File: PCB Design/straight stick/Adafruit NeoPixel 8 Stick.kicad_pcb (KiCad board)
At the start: 2 copper layers, 52.3 x 15.7 mm, 22 parts, among them CN1 1X4SMT, CN2 1X4SMT, J1 2058703-2, J2 2058703-2

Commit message: cleaner routing
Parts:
- removed J1, J2: 2058703-2, 2058703-2:TE_2058703-2
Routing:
- net GND: track 50.3 -> 18.4 mm, vias 10 -> 7
- net +5V: track 113.2 -> 110.4 mm, vias 7 -> 3

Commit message: 4 pin fix
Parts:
- removed C1, C2, C3, C4, C5, C6, C7, C8: C-USC0805K, Adafruit NeoPixel 8 Stick:C0805K
- removed LED1, LED2, LED3, LED4, LED5, LED6, LED7, LED8: >VALUE, Adafruit NeoPixel 8 Stick:WS28115050
- added D1: WS2812B, LED_SMD:LED_WS2812B_PLCC4_5.0x5.0mm_P3.2mm, F.Cu at (126.5, 105.2)
- added D2: WS2812B, LED_SMD:LED_WS2812B_PLCC4_5.0x5.0mm_P3.2mm, F.Cu at (133.6, 105.2)
- added D3: WS2812B, LED_SMD:LED_WS2812B_PLCC4_5.0x5.0mm_P3.2mm, F.Cu at (140.7, 105.2)
- added D4: WS2812B, LED_SMD:LED_WS2812B_PLCC4_5.0x5.0mm_P3.2mm, F.Cu at (147.8, 105.2)
- added D5: WS2812B, LED_SMD:LED_WS2812B_PLCC4_5.0x5.0mm_P3.2mm, F.Cu at (154.9, 105.2)
- added D6: WS2812B, LED_SMD:LED_WS2812B_PLCC4_5.0x5.0mm_P3.2mm, F.Cu at (162.1, 105.2)
- added D7: WS2812B, LED_SMD:LED_WS2812B_PLCC4_5.0x5.0mm_P3.2mm, F.Cu at (169.2, 105.2)
- added D8: WS2812B, LED_SMD:LED_WS2812B_PLCC4_5.0x5.0mm_P3.2mm, F.Cu at (176.3, 105.2)
- moved CN1 5.59 mm to (176.3, 104.4)
- moved FID1 4.70 mm to (133.1, 101.1)
- moved FID3 1.61 mm to (169.7, 101.1)
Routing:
- net +5V: track 110.4 -> 71.8 mm, vias 3 -> 2
- net GND: track 18.4 -> 0.00 mm, vias 7 -> 1
- net Net-(CN1-Pad2): track 18.1 -> 2.63 mm
- net Net-(LED4-PadDO): track 9.64 -> 0.00 mm
- net Net-(LED3-PadDO): track 9.64 -> 0.00 mm
- net Net-(LED2-PadDO): track 9.64 -> 0.00 mm
- net Net-(LED1-PadDO): track 9.64 -> 0.00 mm
- net Net-(LED5-PadDO): track 9.57 -> 0.00 mm
- net Net-(LED7-PadDO): track 9.02 -> 0.00 mm
- net Net-(LED6-PadDO): track 8.87 -> 0.00 mm
- net Net-(D5-Pad2): track 0.00 -> 4.12 mm
- net Net-(D4-Pad2): track 0.00 -> 4.12 mm
- net Net-(D7-Pad2): track 0.00 -> 4.12 mm
- net Net-(D6-Pad2): track 0.00 -> 4.12 mm
- net Net-(D3-Pad2): track 0.00 -> 4.12 mm
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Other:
- board size 52.3 x 15.7 mm -> 57.9 x 15.7 mm

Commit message: 6 pin
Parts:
- removed FID1, FID3: FIDUCIAL"", Adafruit NeoPixel 8 Stick:FIDUCIAL_1MM
- moved CN1 4.06 mm to (176.1, 108.5)
- moved D1 2.79 mm to (126.5, 108.0)
- moved D2 2.79 mm to (133.6, 108.0)
- moved D3 2.79 mm to (140.7, 108.0)
- moved D4 2.79 mm to (147.8, 108.0)
- moved D5 2.79 mm to (154.9, 108.0)
- moved D6 2.79 mm to (162.1, 108.0)
- moved D7 2.79 mm to (169.2, 108.0)
- moved D8 2.79 mm to (176.3, 108.0)
- moved CN2 1.53 mm to (126.9, 107.4)
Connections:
- CN1 pad 1: GND -> Net-(CN1-Pad1)
- CN1 pad 3: +5V -> GND
- CN1 pad 4: GND -> Net-(D8-Pad2)
- D8 pad 2: Net-(CN1-Pad2) -> Net-(D8-Pad2)
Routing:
- net Net-(CN1-Pad1): track 0.00 -> 55.1 mm
- net Net-(CN1-Pad2): track 2.63 -> 51.8 mm, vias 1 -> 0
- net Net-(D8-Pad2): track 0.00 -> 4.79 mm, vias 0 -> 1
- net Net-(CN2-Pad3): track 4.35 -> 0.00 mm
- net +5V: track 71.8 -> 68.3 mm
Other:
- board size 57.9 x 15.7 mm -> 58.2 x 21 mm
- board text removed: "4-7VDC"
- board text removed: "DIN"
- board text removed: "DOUT"
- board text removed: "GND"

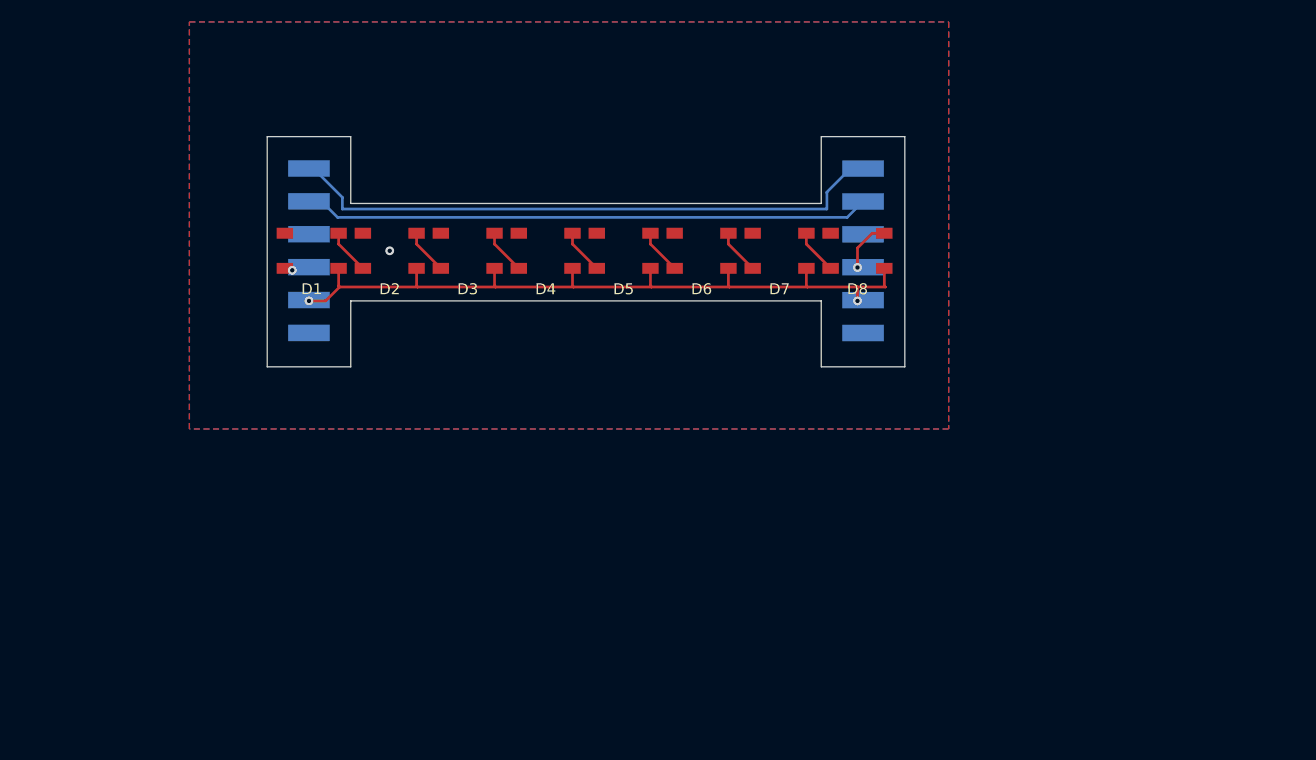
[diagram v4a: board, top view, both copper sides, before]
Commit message: half size straight stick
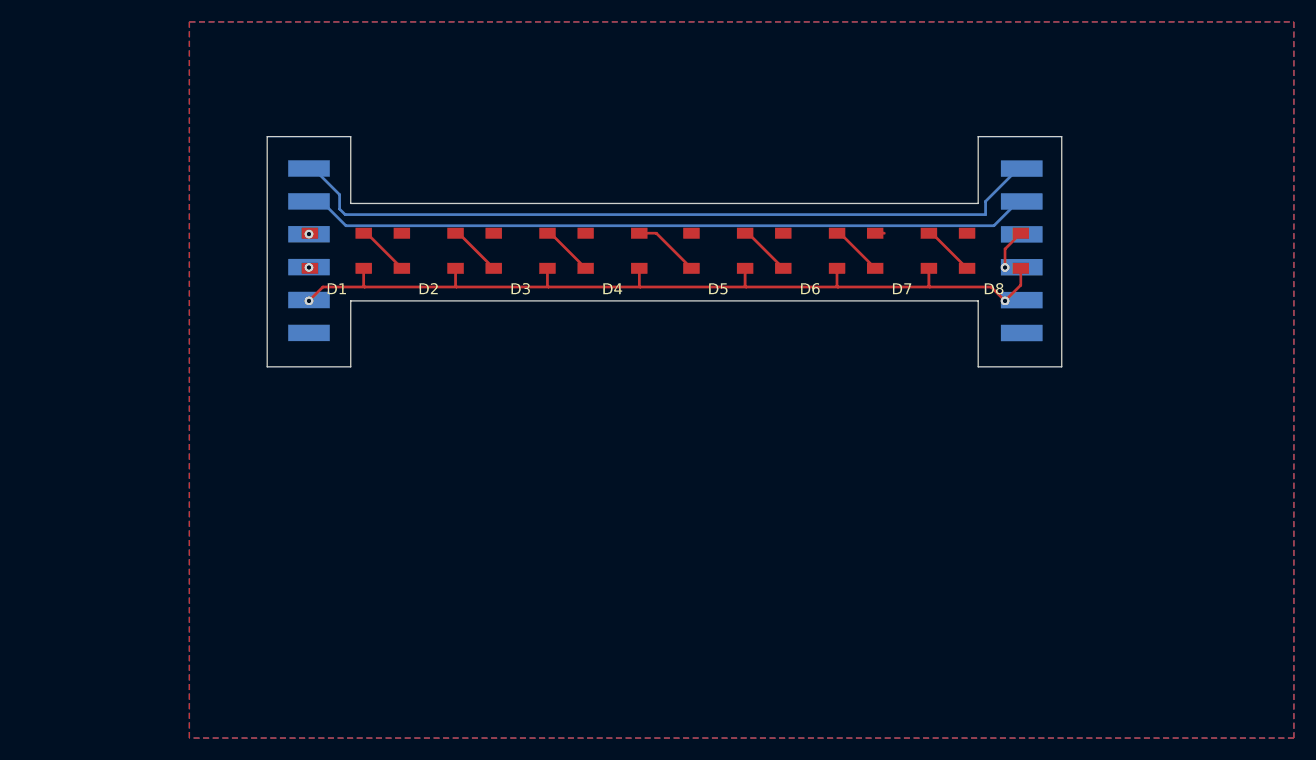
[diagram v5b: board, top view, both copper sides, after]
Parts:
- moved CN1 14.5 mm to (190.6, 108.5)
- moved D8 12.4 mm to (188.7, 108.0)
- moved D7 11.2 mm to (180.3, 108.0)
- moved D6 9.91 mm to (172.0, 108.0)
- moved D5 8.64 mm to (163.6, 108.0)
- moved D4 6.10 mm to (153.9, 108.0)
- moved D3 4.83 mm to (145.5, 108.0)
- moved D2 3.56 mm to (137.2, 108.0)
- moved D1 2.29 mm to (128.8, 108.0)
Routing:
- net Net-(CN1-Pad2): track 51.8 -> 66.9 mm
- net Net-(CN1-Pad1): track 55.1 -> 70.0 mm
- net +5V: track 68.3 -> 80.3 mm
- net Net-(D4-Pad2): track 4.12 -> 6.08 mm
- net GND: track 0.00 -> 1.10 mm
- net Net-(D8-Pad2): track 4.79 -> 3.72 mm
- net Net-(D7-Pad2): track 4.12 -> 4.81 mm
- net Net-(D6-Pad2): track 4.12 -> 4.81 mm
- net Net-(D3-Pad2): track 4.12 -> 4.81 mm
- net Net-(D2-Pad2): track 4.12 -> 4.81 mm
- net Net-(D1-Pad2): track 4.12 -> 4.81 mm
- net Net-(D5-Pad2): track 4.12 -> 4.81 mm
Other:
- board size 58.2 x 21 mm -> 72.5 x 21 mm

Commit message: clean up boards + generate some gerber files
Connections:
- net Net-(CN1-Pad1) renamed /SCL
- net Net-(CN1-Pad2) renamed /SDA
- net Net-(CN2-Pad3) renamed /LED DATA
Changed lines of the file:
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@@
       (outputformat 1)
       (mirror false)
-      (drillshape 1)
+      (drillshape 0)
       (scaleselection 1)
-      (outputdirectory "")
+      (outputdirectory "gerbers/")
     )
   )
@@
   (net 1 "+5V")
   (net 2 "GND")
-  (net 3 "Net-(CN1-Pad2)")
-  (net 4 "Net-(CN2-Pad3)")
+  (net 3 "/SCL")
+  (net 4 "/SDA")
   (net 5 "Net-(D1-Pad2)")
   (net 6 "Net-(D2-Pad2)")
@@
   (net 11 "Net-(D7-Pad2)")
   (net 12 "Net-(D8-Pad2)")
-  (net 13 "Net-(CN1-Pad1)")
+  (net 13 "/LED DATA")
   (footprint "LED_SMD:LED_WS2812B_PLCC4_5.0x5.0mm_P3.2mm" (layer "F.Cu")
     (at 163.576 107.95 180)
@@
       (net 2 "GND") (pinfunction "VSS") (pintype "power_in"))
     (pad "4" smd rect (at 2.45 -1.6 180) (size 1.5 1) (layers "F.Cu" "F.Paste" "F.Mask")
-      (net 4 "Net-(CN2-Pad3)") (pinfunction "DIN") (pintype "input"))
+      (net 13 "/LED DATA") (pinfunction "DIN") (pintype "input"))
     (model "${KICAD6_3DMODEL_DIR}/LED_SMD.3dshapes/LED_WS2812B_PLCC4_5.0x5.0mm_P3.2mm.wrl"
       (offset (xyz 0 0 0))
@@
       (net 1 "+5V") (pinfunction "2") (pintype "bidirectional") (solder_mask_margin 0.1016))
     (pad "3" smd rect (at -2 -0.635 90) (size 1.5 3.8) (layers "B.Cu" "B.Paste" "B.Mask")
-      (net 4 "Net-(CN2-Pad3)") (pinfunction "3") (pintype "bidirectional") (solder_mask_margin 0.1016))
+      (net 13 "/LED DATA") (pinfunction "3") (pintype "bidirectional") (solder_mask_margin 0.1016))
     (pad "4" smd rect (at 1 -0.635 90) (size 1.5 3.8) (layers "B.Cu" "B.Paste" "B.Mask")
       (net 2 "GND") (pinfunction "4") (pintype "bidirectional") (solder_mask_margin 0.1016))
     (pad "5" smd rect (at 4 -0.635 90) (size 1.5 3.8) (layers "B.Cu" "B.Paste" "B.Mask")
-      (net 3 "Net-(CN1-Pad2)") (pinfunction "5") (pintype "bidirectional") (solder_mask_margin 0.1016))
+      (net 4 "/SDA") (pinfunction "5") (pintype "bidirectional") (solder_mask_margin 0.1016))
     (pad "6" smd rect (at 7 -0.635 90) (size 1.5 3.8) (layers "B.Cu" "B.Paste" "B.Mask")
-      (net 13 "Net-(CN1-Pad1)") (pinfunction "6") (pintype "bidirectional") (solder_mask_margin 0.1016))
+      (net 3 "/SCL") (pinfunction "6") (pintype "bidirectional") (solder_mask_margin 0.1016))
   )
   (footprint "Adafruit NeoPixel 8 Stick:1X4-SMT" (layer "B.Cu")
@@
     )
     (pad "1" smd rect (at -8 -0.635 270) (size 1.5 3.8) (layers "B.Cu" "B.Paste" "B.Mask")
-      (net 13 "Net-(CN1-Pad1)") (pinfunction "1") (pintype "bidirectional") (solder_mask_margin 0.1016))
+      (net 3 "/SCL") (pinfunction "1") (pintype "bidirectional") (solder_mask_margin 0.1016))
     (pad "2" smd rect (at -5 -0.635 270) (size 1.5 3.8) (layers "B.Cu" "B.Paste" "B.Mask")
-      (net 3 "Net-(CN1-Pad2)") (pinfunction "2") (pintype "bidirectional") (solder_mask_margin 0.1016))
+      (net 4 "/SDA") (pinfunction "2") (pintype "bidirectional") (solder_mask_margin 0.1016))
     (pad "3" smd rect (at -2 -0.635 270) (size 1.5 3.8) (layers "B.Cu" "B.Paste" "B.Mask")
       (net 2 "GND") (pinfunction "3") (pintype "bidirectional") (solder_mask_margin 0.1016))
@@
   (segment (start 178.726 106.35) (end 177.622 106.35) (width 0.25) (layer "F.Cu") (net 2))
   (via (at 126.238 106.426) (size 0.8) (drill 0.4) (layers "F.Cu" "B.Cu") (net 2))
-  (segment (start 126.238 103.442) (end 127.388 103.442) (width 0.25) (layer "B.Cu") (net 3))
-  (segment (start 190.936 103.45) (end 191.262 103.45) (width 0.25) (layer "B.Cu") (net 3))
-  (segment (start 129.61 105.664) (end 188.722 105.664) (width 0.25) (layer "B.Cu") (net 3))
-  (segment (start 188.722 105.664) (end 190.936 103.45) (width 0.25) (layer "B.Cu") (net 3))
-  (segment (start 127.388 103.442) (end 129.61 105.664) (width 0.25) (layer "B.Cu") (net 3))
-  (via (at 126.238 109.474) (size 0.8) (drill 0.4) (layers "F.Cu" "B.Cu") (net 4))
+  (segment (start 187.96 103.4456) (end 190.9556 100.45) (width 0.25) (layer "B.Cu") (net 3))
+  (segment (start 190.9556 100.45) (end 191.262 100.45) (width 0.25) (layer "B.Cu") (net 3))
+  (segment (start 126.238 100.442) (end 126.645868 100.442) (width 0.25) (layer "B.Cu") (net 3))
+  (segment (start 129.54 104.648) (end 187.96 104.648) (width 0.25) (layer "B.Cu") (net 3))
+  (segment (start 187.96 104.648) (end 187.96 103.4456) (width 0.25) (layer "B.Cu") (net 3))
+  (segment (start 129.032 102.828132) (end 129.032 104.14) (width 0.25) (layer "B.Cu") (net 3))
+  (segment (start 126.645868 100.442) (end 129.032 102.828132) (width 0.25) (layer "B.Cu") (net 3))
+  (segment (start 129.032 104.14) (end 129.54 104.648) (width 0.25) (layer "B.Cu") (net 3))
+  (segment (start 126.238 103.442) (end 127.388 103.442) (width 0.25) (layer "B.Cu") (net 4))
+  (segment (start 190.936 103.45) (end 191.262 103.45) (width 0.25) (layer "B.Cu") (net 4))
+  (segment (start 129.61 105.664) (end 188.722 105.664) (width 0.25) (layer "B.Cu") (net 4))
+  (segment (start 188.722 105.664) (end 190.936 103.45) (width 0.25) (layer "B.Cu") (net 4))
+  (segment (start 127.388 103.442) (end 129.61 105.664) (width 0.25) (layer "B.Cu") (net 4))
   (segment (start 131.228 106.35) (end 131.51 106.35) (width 0.25) (layer "F.Cu") (net 5))
   (segment (start 131.51 106.35) (end 134.71 109.55) (width 0.25) (layer "F.Cu") (net 5))
@@
   (segment (start 189.738 107.784) (end 191.172 106.35) (width 0.25) (layer "F.Cu") (net 12))
   (via (at 189.738 109.474) (size 0.8) (drill 0.4) (layers "F.Cu" "B.Cu") (net 12))
-  (segment (start 187.96 103.4456) (end 190.9556 100.45) (width 0.25) (layer "B.Cu") (net 13))
-  (segment (start 190.9556 100.45) (end 191.262 100.45) (width 0.25) (layer "B.Cu") (net 13))
-  (segment (start 126.238 100.442) (end 126.645868 100.442) (width 0.25) (layer "B.Cu") (net 13))
-  (segment (start 129.54 104.648) (end 187.96 104.648) (width 0.25) (layer "B.Cu") (net 13))
-  (segment (start 187.96 104.648) (end 187.96 103.4456) (width 0.25) (layer "B.Cu") (net 13))
-  (segment (start 129.032 102.828132) (end 129.032 104.14) (width 0.25) (layer "B.Cu") (net 13))
-  (segment (start 126.645868 100.442) (end 129.032 102.828132) (width 0.25) (layer "B.Cu") (net 13))
-  (segment (start 129.032 104.14) (end 129.54 104.648) (width 0.25) (layer "B.Cu") (net 13))
+  (via (at 126.238 109.474) (size 0.8) (drill 0.4) (layers "F.Cu" "B.Cu") (net 13))
   (zone (net 2) (net_name "GND") (layers F&B.Cu) (hatch edge 0.508)
     (priority 6)

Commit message: rm vias over pads
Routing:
- net /LED DATA: track 0.00 -> 6.23 mm
- net GND: track 1.10 -> 7.33 mm
- net Net-(CN1-Pad4): track 3.72 -> 7.29 mm
- net /SDA: track 66.9 -> 65.4 mm
- net +5V: track 80.3 -> 81.6 mm
- net /SCL: track 70.0 -> 69.3 mm
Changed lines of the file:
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@@
   (net 10 "Net-(D6-Pad2)")
   (net 11 "Net-(D7-Pad2)")
-  (net 12 "Net-(D8-Pad2)")
+  (net 12 "Net-(CN1-Pad4)")
   (net 13 "/LED DATA")
   (footprint "LED_SMD:LED_WS2812B_PLCC4_5.0x5.0mm_P3.2mm" (layer "F.Cu")
@@
       (net 1 "+5V") (pinfunction "VDD") (pintype "power_in"))
     (pad "2" smd rect (at -2.45 1.6 180) (size 1.5 1) (layers "F.Cu" "F.Paste" "F.Mask")
-      (net 12 "Net-(D8-Pad2)") (pinfunction "DOUT") (pintype "output"))
+      (net 12 "Net-(CN1-Pad4)") (pinfunction "DOUT") (pintype "output"))
     (pad "3" smd rect (at 2.45 1.6 180) (size 1.5 1) (layers "F.Cu" "F.Paste" "F.Mask")
       (net 2 "GND") (pinfunction "VSS") (pintype "power_in"))
@@
       (net 2 "GND") (pinfunction "3") (pintype "bidirectional") (solder_mask_margin 0.1016))
     (pad "4" smd rect (at 1 -0.635 270) (size 1.5 3.8) (layers "B.Cu" "B.Paste" "B.Mask")
-      (net 12 "Net-(D8-Pad2)") (pinfunction "4") (pintype "bidirectional") (solder_mask_margin 0.1016))
+      (net 12 "Net-(CN1-Pad4)") (pinfunction "4") (pintype "bidirectional") (solder_mask_margin 0.1016))
     (pad "5" smd rect (at 4 -0.635 270) (size 1.5 3.8) (layers "B.Cu" "B.Paste" "B.Mask")
       (net 1 "+5V") (pinfunction "5") (pintype "bidirectional") (solder_mask_margin 0.1016))
@@
   (segment (start 139.61 111.162) (end 139.7 111.252) (width 0.25) (layer "F.Cu") (net 1))
   (segment (start 127.508 111.252) (end 131.318 111.252) (width 0.25) (layer "F.Cu") (net 1))
-  (segment (start 189.738 112.522) (end 191.172 111.088) (width 0.25) (layer "F.Cu") (net 1))
   (segment (start 182.79 109.55) (end 182.79 111.162) (width 0.25) (layer "F.Cu") (net 1))
   (segment (start 148.082 111.252) (end 156.464 111.252) (width 0.25) (layer "F.Cu") (net 1))
@@
   (segment (start 147.992 109.55) (end 147.992 111.162) (width 0.25) (layer "F.Cu") (net 1))
   (segment (start 131.318 111.252) (end 139.7 111.252) (width 0.25) (layer "F.Cu") (net 1))
-  (segment (start 191.172 111.088) (end 191.172 109.55) (width 0.25) (layer "F.Cu") (net 1))
   (segment (start 156.374 111.162) (end 156.464 111.252) (width 0.25) (layer "F.Cu") (net 1))
   (segment (start 139.61 109.55) (end 139.61 111.162) (width 0.25) (layer "F.Cu") (net 1))
   (segment (start 182.88 111.252) (end 188.468 111.252) (width 0.25) (layer "F.Cu") (net 1))
-  (segment (start 188.468 111.252) (end 189.738 112.522) (width 0.25) (layer "F.Cu") (net 1))
+  (segment (start 190.17 109.55) (end 191.172 109.55) (width 0.25) (layer "F.Cu") (net 1))
   (segment (start 147.992 111.162) (end 148.082 111.252) (width 0.25) (layer "F.Cu") (net 1))
   (segment (start 174.498 111.252) (end 182.88 111.252) (width 0.25) (layer "F.Cu") (net 1))
@@
   (segment (start 174.408 111.162) (end 174.498 111.252) (width 0.25) (layer "F.Cu") (net 1))
   (segment (start 131.228 111.162) (end 131.318 111.252) (width 0.25) (layer "F.Cu") (net 1))
+  (segment (start 188.468 111.252) (end 190.17 109.55) (width 0.25) (layer "F.Cu") (net 1))
   (segment (start 174.408 109.55) (end 174.408 111.162) (width 0.25) (layer "F.Cu") (net 1))
   (segment (start 182.79 111.162) (end 182.88 111.252) (width 0.25) (layer "F.Cu") (net 1))
   (via (at 126.238 112.522) (size 0.8) (drill 0.4) (layers "F.Cu" "B.Cu") (net 1))
-  (via (at 189.738 112.522) (size 0.8) (drill 0.4) (layers "F.Cu" "B.Cu") (net 1))
+  (via (at 188.468 111.252) (size 0.8) (drill 0.4) (layers "F.Cu" "B.Cu") (net 1))
+  (segment (start 188.468 111.252) (end 189.666 112.45) (width 0.25) (layer "B.Cu") (net 1))
+  (segment (start 189.666 112.45) (end 191.262 112.45) (width 0.25) (layer "B.Cu") (net 1))
+  (segment (start 123.266 106.35) (end 123.19 106.426) (width 0.25) (layer "F.Cu") (net 2))
   (segment (start 178.726 106.35) (end 177.622 106.35) (width 0.25) (layer "F.Cu") (net 2))
-  (via (at 126.238 106.426) (size 0.8) (drill 0.4) (layers "F.Cu" "B.Cu") (net 2))
+  (segment (start 126.328 106.35) (end 123.266 106.35) (width 0.25) (layer "F.Cu") (net 2))
+  (via (at 123.19 106.426) (size 0.8) (drill 0.4) (layers "F.Cu" "B.Cu") (net 2))
+  (segment (start 123.206 106.442) (end 126.238 106.442) (width 0.25) (layer "B.Cu") (net 2))
+  (segment (start 123.19 106.426) (end 123.206 106.442) (width 0.25) (layer "B.Cu") (net 2))
   (segment (start 187.96 103.4456) (end 190.9556 100.45) (width 0.25) (layer "B.Cu") (net 3))
-  (segment (start 190.9556 100.45) (end 191.262 100.45) (width 0.25) (layer "B.Cu") (net 3))
-  (segment (start 126.238 100.442) (end 126.645868 100.442) (width 0.25) (layer "B.Cu") (net 3))
   (segment (start 129.54 104.648) (end 187.96 104.648) (width 0.25) (layer "B.Cu") (net 3))
   (segment (start 187.96 104.648) (end 187.96 103.4456) (width 0.25) (layer "B.Cu") (net 3))
@@
   (segment (start 126.645868 100.442) (end 129.032 102.828132) (width 0.25) (layer "B.Cu") (net 3))
   (segment (start 129.032 104.14) (end 129.54 104.648) (width 0.25) (layer "B.Cu") (net 3))
-  (segment (start 126.238 103.442) (end 127.388 103.442) (width 0.25) (layer "B.Cu") (net 4))
-  (segment (start 190.936 103.45) (end 191.262 103.45) (width 0.25) (layer "B.Cu") (net 4))
   (segment (start 129.61 105.664) (end 188.722 105.664) (width 0.25) (layer "B.Cu") (net 4))
   (segment (start 188.722 105.664) (end 190.936 103.45) (width 0.25) (layer "B.Cu") (net 4))
   (segment (start 127.388 103.442) (end 129.61 105.664) (width 0.25) (layer "B.Cu") (net 4))
-  (segment (start 131.228 106.35) (end 131.51 106.35) (width 0.25) (layer "F.Cu") (net 5))
   (segment (start 131.51 106.35) (end 134.71 109.55) (width 0.25) (layer "F.Cu") (net 5))
-  (segment (start 139.61 106.35) (end 139.892 106.35) (width 0.25) (layer "F.Cu") (net 6))
   (segment (start 139.892 106.35) (end 143.092 109.55) (width 0.25) (layer "F.Cu") (net 6))
   (segment (start 148.274 106.35) (end 151.474 109.55) (width 0.25) (layer "F.Cu") (net 7))
-  (segment (start 147.992 106.35) (end 148.274 106.35) (width 0.25) (layer "F.Cu") (net 7))
   (segment (start 156.374 106.35) (end 157.926 106.35) (width 0.25) (layer "F.Cu") (net 8))
   (segment (start 157.926 106.35) (end 161.126 109.55) (width 0.25) (layer "F.Cu") (net 8))
   (segment (start 166.308 106.35) (end 169.508 109.55) (width 0.25) (layer "F.Cu") (net 9))
-  (segment (start 166.026 106.35) (end 166.308 106.35) (width 0.25) (layer "F.Cu") (net 9))
-  (segment (start 174.408 106.35) (end 174.69 106.35) (width 0.25) (layer "F.Cu") (net 10))
   (segment (start 174.69 106.35) (end 177.89 109.55) (width 0.25) (layer "F.Cu") (net 10))
-  (segment (start 182.79 106.35) (end 183.072 106.35) (width 0.25) (layer "F.Cu") (net 11))
   (segment (start 183.072 106.35) (end 186.272 109.55) (width 0.25) (layer "F.Cu") (net 11))
-  (segment (start 189.738 109.474) (end 189.738 107.784) (width 0.25) (layer "F.Cu") (net 12))
-  (segment (start 189.738 107.784) (end 191.172 106.35) (width 0.25) (layer "F.Cu") (net 12))
-  (via (at 189.738 109.474) (size 0.8) (drill 0.4) (layers "F.Cu" "B.Cu") (net 12))
-  (via (at 126.238 109.474) (size 0.8) (drill 0.4) (layers "F.Cu" "B.Cu") (net 13))
+  (segment (start 191.172 106.35) (end 190.068 106.35) (width 0.25) (layer "F.Cu") (net 12))
+  (segment (start 190.068 106.35) (end 188.214 108.204) (width 0.25) (layer "F.Cu") (net 12))
+  (via (at 188.214 108.204) (size 0.8) (drill 0.4) (layers "F.Cu" "B.Cu") (net 12))
+  (segment (start 189.46 109.45) (end 191.262 109.45) (width 0.25) (layer "B.Cu") (net 12))
+  (segment (start 188.214 108.204) (end 189.46 109.45) (width 0.25) (layer "B.Cu") (net 12))
+  (segment (start 123.266 109.55) (end 123.19 109.474) (width 0.25) (layer "F.Cu") (net 13))
+  (segment (start 126.328 109.55) (end 123.266 109.55) (width 0.25) (layer "F.Cu") (net 13))
+  (via (at 123.19 109.474) (size 0.8) (drill 0.4) (layers "F.Cu" "B.Cu") (net 13))
+  (segment (start 123.19 109.474) (end 123.222 109.442) (width 0.25) (layer "B.Cu") (net 13))
+  (segment (start 123.222 109.442) (end 126.238 109.442) (width 0.25) (layer "B.Cu") (net 13))
   (zone (net 2) (net_name "GND") (layers F&B.Cu) (hatch edge 0.508)
     (priority 6)
